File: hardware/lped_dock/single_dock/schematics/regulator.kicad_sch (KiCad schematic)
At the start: 9 parts, among them U2 TPS560200

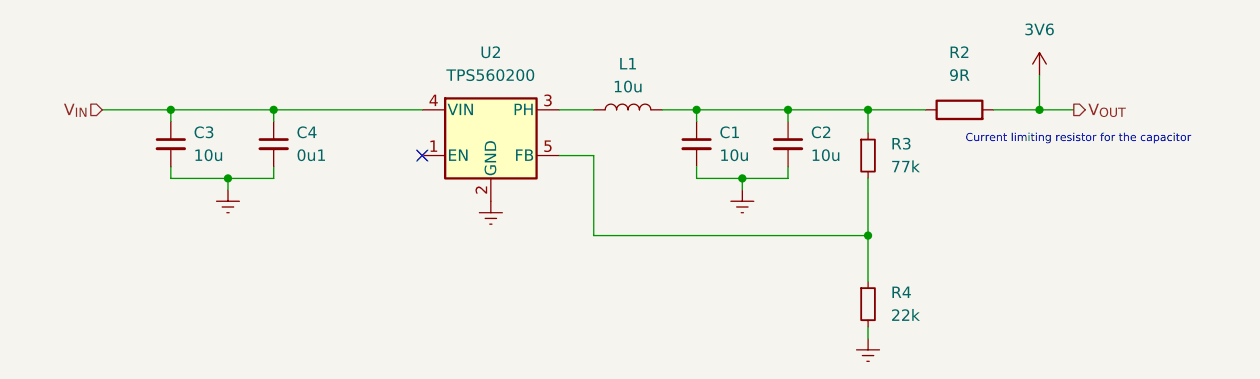
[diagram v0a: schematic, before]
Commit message: feat(hardware): change regulator, add mounting hole to single charger
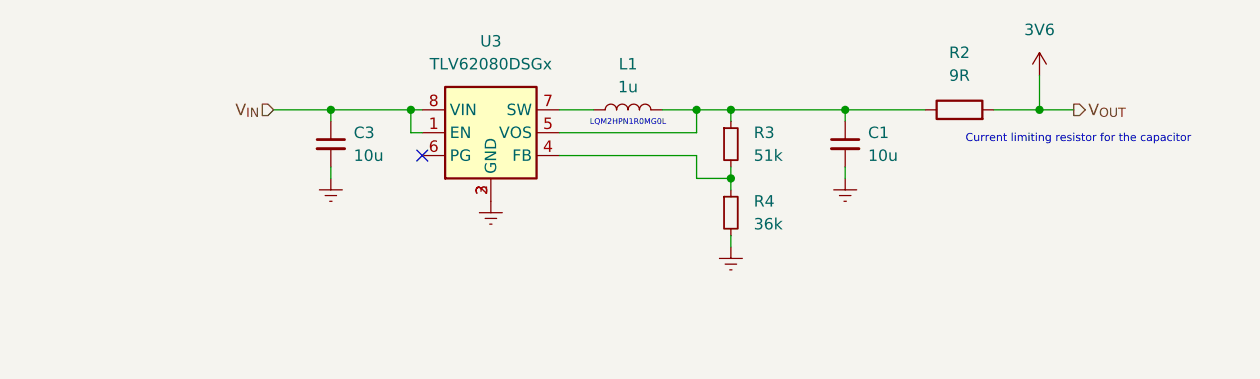
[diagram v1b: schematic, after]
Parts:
- removed C2: 10u, Capacitor_SMD:C_0603_1608Metric, symbol Device:C_Small
- removed C4: 0u1, Capacitor_SMD:C_0402_1005Metric, symbol Device:C_Small
- removed U2: TPS560200, Package_TO_SOT_SMD:SOT-23-5, symbol Regulator_Switching:TPS560200
- added U3: TLV62080DSGx, Package_SON:WSON-8-1EP_2x2mm_P0.5mm_EP0.9x1.6mm, symbol Regulator_Switching:TLV62080DSGx
- L1: value 10u -> 1u; footprint Inductor_SMD:L_0805_2012Metric -> Inductor_SMD:L_1008_2520Metric
- R3: value 77k -> 51k
- R4: value 22k -> 36k
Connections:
- net Earth: now also U3.2 (GND), U3.3 (GND), U3.9 (GND)
- net V_{IN}: now also U3.1 (EN), U3.8 (VIN)
- net at C1.1, L1.2, R2.1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: now also U3.5 (VOS)
- net at R3.2, R4.1: now also U3.4 (FB)
- net at L1.1: now also U3.7 (SW)
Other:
- note added: "LQM2HPN1R0MG0L"
- moved on the sheet: C1, C3, R3, R4
